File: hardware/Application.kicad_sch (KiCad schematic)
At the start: 32 parts, among them J501 Conn_ARM_SWD_TagConnect_TC203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, J502 Conn_ARM_SWD_TagConnect_TC2030, J503 BOOT0, U501 STM32G431CBU6, U502 W25X10CLUXIG, Y501 32_Mhz

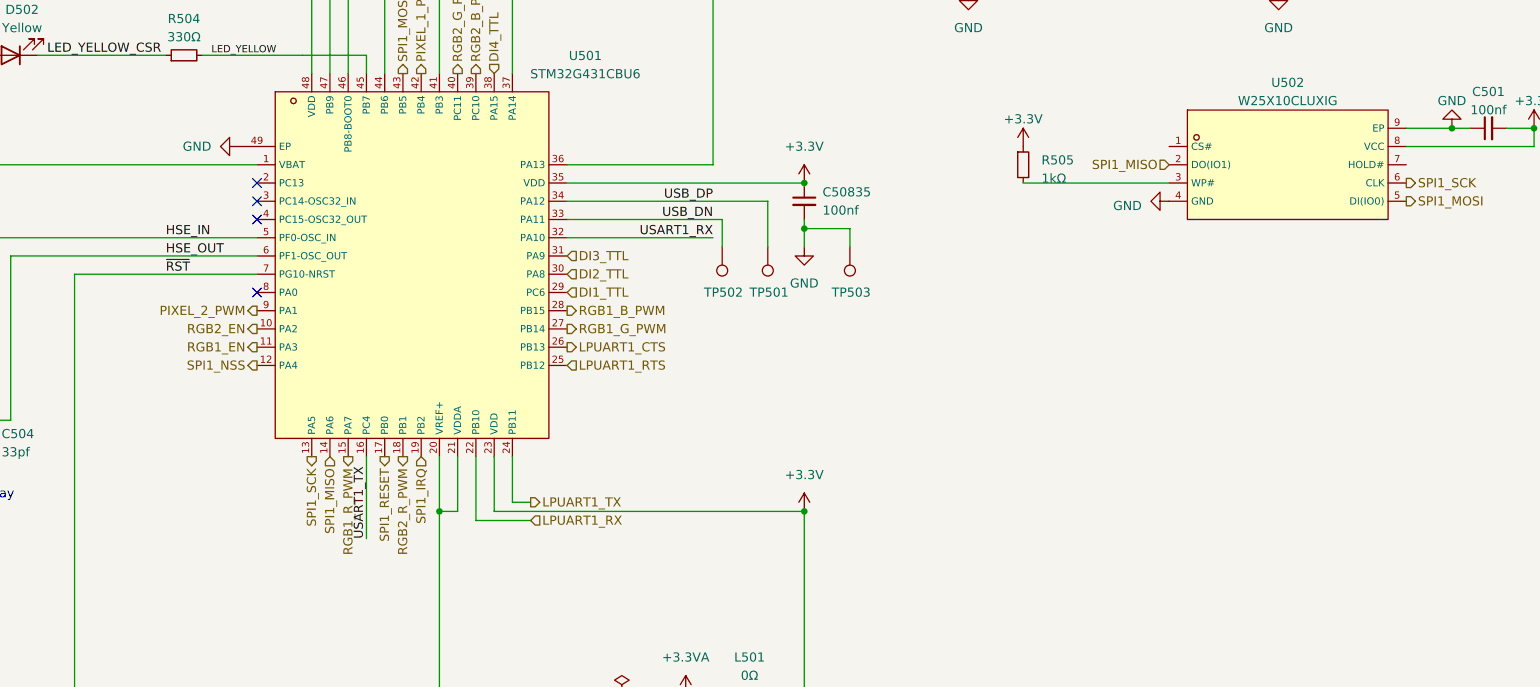
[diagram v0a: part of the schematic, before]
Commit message: hardware: add USB for debugging and programming
Signed-off-by: Connor Rigby <connorr@hey.com>
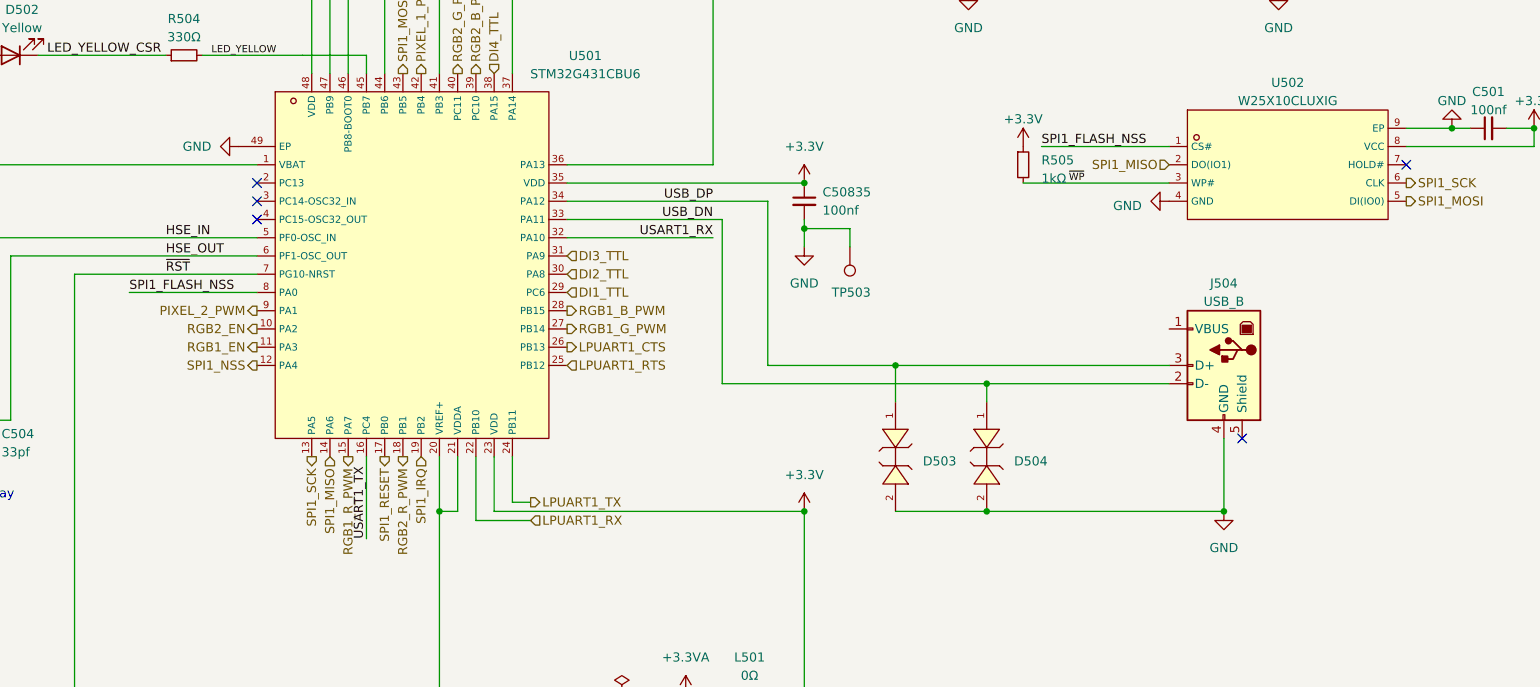
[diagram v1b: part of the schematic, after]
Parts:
- removed TP501: DP, TestPoint:TestPoint_Pad_D1.0mm, symbol Connector:TestPoint
- removed TP502: DN, TestPoint:TestPoint_Pad_D1.0mm, symbol Connector:TestPoint
- added D503, D504: ESD9B3_3ST5G, LCSC_ESD:SOD-923_L0.8-W0.6-LS1.0-BI-1, symbol LCSC_ESD:ESD9B3_3ST5G
- added J504: USB_B, LCSC_Connector:USB-B-TH_67068-8000, symbol Connector:USB_B
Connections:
- net GND: now also D503.2, D504.2, J504.4 (GND)
- net USB_DN: now also D504.1, J504.2 (D-)
- net USB_DP: now also D503.1, J504.3 (D+)
- net SPI1_FLASH_NSS: now reaches U502.1 (CS#)
- net SPI1_FLASH_NSS: now also U501.8 (PA0)
- net ~{WP}: now reaches R505.2, U502.3 (WP#)
- no-connect marks 8 -> 9

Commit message: Rev 2 submitted for production
Signed-off-by: Connor Rigby <connorr@hey.com>
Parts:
- removed BTN501, BTN502: GT-TC029B-H025-L1N, Button:SW-SMD_L3.9-W3.0-P4.45, symbol LCSC_Tactile_Switch:GT-TC029B-H025-L1N
- removed C501, C50823, C50835, C50848: C_0402_100nf_X7R, Capacitor_SMD:C_0402_1005Metric, symbol LCSC_Capacitor:C_0402_100nf_X7R
- removed C503, C504: C_0402_33p_C0G, Capacitor_SMD:C_0402_1005Metric, symbol LCSC_Capacitor:C_0402_33p_C0G
- removed C506: C_0402_1u_X5R, Capacitor_SMD:C_0402_1005Metric, symbol LCSC_Capacitor:C_0402_1u_X5R
- removed C509: C_0805_10u_X5R, Capacitor_SMD:C_0805_2012Metric, symbol LCSC_Capacitor:C_0805_10u_X5R
- removed D501: LED_0603_GREEN, LED_SMD:LED_0603_1608Metric, symbol LCSC_LED:LED_0603_GREEN
- removed D502: LED_0603_YELLOW, LED_SMD:LED_0603_1608Metric, symbol LCSC_LED:LED_0603_YELLOW
- removed D503, D504: ESD9B3_3ST5G, LCSC_ESD:SOD-923_L0.8-W0.6-LS1.0-BI-1, symbol LCSC_ESD:ESD9B3_3ST5G
- removed J501: Conn_ARM_SWD_TagConnect_TC2030-NL, Connector:Tag-Connect_TC2030-IDC-NL_2x03_P1.27mm_Vertical, symbol Connector:Conn_ARM_SWD_TagConnect_TC2030-NL
- removed J502: Conn_ARM_SWD_TagConnect_TC2030, Connector:Tag-Connect_TC2030-IDC-FP_2x03_P1.27mm_Vertical, symbol Connector:Conn_ARM_SWD_TagConnect_TC2030
- removed J503: BOOT0, Connector_PinHeader_2.54mm:PinHeader_1x02_P2.54mm_Vertical, symbol Connector_Generic:Conn_01x02
- removed J504: USB_B, LCSC_Connector:USB-B-TH_67068-8000, symbol Connector:USB_B
- removed L501: R_0402_0, Resistor_SMD:R_0402_1005Metric, symbol LCSC_Resistor:R_0402_0
- removed R501, R505: R_0402_1k, Resistor_SMD:R_0402_1005Metric, symbol LCSC_Resistor:R_0402_1k
- removed R502: R_0402_10k, Resistor_SMD:R_0402_1005Metric, symbol LCSC_Resistor:R_0402_10k
- removed R503, R504: R_0603_330, Resistor_SMD:R_0603_1608Metric, symbol LCSC_Resistor:R_0603_330
- removed TP503: GND, TestPoint:TestPoint_Pad_D1.0mm, symbol Connector:TestPoint
- removed U501: STM32G431CBU6, LCSC_Microcontroller:QFN50P700X700X60-49N, symbol LCSC_Microcontroller:STM32G431CBU6
- removed U502: W25X10CLUXIG, LCSC_Microcontroller:USON-8_L3.0-W2.0-P0.50-BL-EP-1, symbol LCSC_Microcontroller:W25X10CLUXIG
- removed Y501: 32_Mhz, Crystal:Crystal_SMD_3225-4Pin_3.2x2.5mm, symbol LCSC_Crystal:32_Mhz
- added BT501: Battery_Cell, LCSC_Connector:BAT-SMD_CR1220-2, symbol Device:Battery_Cell
- added C501: C_0805_4u7_X5R, Capacitor_SMD:C_0805_2012Metric, symbol LCSC_Capacitor:C_0805_4u7_X5R
- added C502, C503, C504, C506, C509, C516, C519, C520, C521: C_0402_100nf_X7R, Capacitor_SMD:C_0402_1005Metric, symbol LCSC_Capacitor:C_0402_100nf_X7R
- added C512, C513: C_0402_2u2_X5R, Capacitor_SMD:C_0402_1005Metric, symbol LCSC_Capacitor:C_0402_2u2_X5R
- added C811 (x4): C_0402_22p_C0G, Capacitor_SMD:C_0402_1005Metric, symbol LCSC_Capacitor:C_0402_22p_C0G
- added D202: 30v 230mv@100ma 1A, Diode_SMD:D_SOD-323F, symbol Device:D_Schottky
- added D501: BAT54C, Package_TO_SOT_SMD:SOT-23, symbol Diode:BAT54C
- added D502: LED_0603_GREEN, LED_SMD:LED_0603_1608Metric, symbol LCSC_LED:LED_0603_GREEN
- added D503: LED_0603_YELLOW, LED_SMD:LED_0603_1608Metric, symbol LCSC_LED:LED_0603_YELLOW
- added D504, D506: LED_0603_RED, LED_SMD:LED_0603_1608Metric, symbol LCSC_LED:LED_0603_RED
- added FB501: FerriteBead_Small, Inductor_SMD:L_0402_1005Metric, symbol Device:FerriteBead_Small
- added J501: Conn_ST_STDC14, LCSC_Connector:TC2070-IDC-FP, symbol Connector:Conn_ST_STDC14
- added JP501: SolderJumper_3_Open, Jumper:SolderJumper-3_P1.3mm_Open_RoundedPad1.0x1.5mm_NumberLabels, symbol Jumper:SolderJumper_3_Open
- added R501: R_0402_100k, Resistor_SMD:R_0402_1005Metric, symbol LCSC_Resistor:R_0402_100k
- added R502: R_0402_0, Resistor_SMD:R_0402_1005Metric, symbol LCSC_Resistor:R_0402_0
- added R503, R504, R505: R_0402_10k, Resistor_SMD:R_0402_1005Metric, symbol LCSC_Resistor:R_0402_10k
- added R506, R507, R508, R509: R_0603_330, Resistor_SMD:R_0603_1608Metric, symbol LCSC_Resistor:R_0603_330
- added RN501, RN502, RN503, RN504: RA_0402_04_100, Resistor_SMD:R_Array_Concave_4x0402, symbol LCSC_Resistor:RA_0402_04_100
- added U501: W25Q16JVSSIQ, Package_SO:SOIC-8_5.23x5.23mm_P1.27mm, symbol LCSC_Microcontroller:W25Q16JVSSIQ
- added U503: STM32F407VGTx, Package_QFP:LQFP-100_14x14mm_P0.5mm, symbol MCU_ST_STM32F4:STM32F407VGTx
- added Y501: 25_Mhz, Crystal:Crystal_SMD_3225-4Pin_3.2x2.5mm, symbol LCSC_Crystal:25_Mhz
- added Y502: Q13FC1350000400, Crystal:Crystal_SMD_3215-2Pin_3.2x1.5mm, symbol LCSC_Crystal:Q13FC1350000400
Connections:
- net +3.3V is gone; now on net GND: C508.2
- net BOOT0: now also R501.1, U503.94 (BOOT0)
- net CAN_RX: now also U503.91 (PB5)
- net CAN_TX: now also U503.52 (PB13)
- net GND: now also C507.2, C511.2, BT501.2 (-), C501.2, C502.2, C503.2, C504.2, C506.2, C509.2, C512.1, C513.1, C516.2, C519.2, C520.2, C521.2, C811.1, C811.1, C811.1, C811.1, J501.11 (GNDDetect), J501.5 (GND), J501.7 (GND), R501.2, U501.4 (GND), U503.10 (VSS), U503.20 (VSSA), U503.27 (VSS), U503.74 (VSS), U503.99 (VSS), Y501.2, Y501.4; no longer C507.1, C508.1, C511.1
- net USART1_RX: now also J501.13 (VCP_RX), U503.69 (PA10)
- net USART1_TX: now also J501.14 (VCP_TX), U503.68 (PA9)
- net ~{RST}: now also C516.1, JP501.3 (B), U503.14 (NRST); no longer C505.1
- removed net +3.3VA: C507.2, C510.1, C511.2
- new net: D504.2 (A), R509.1
- new net: C520.1, D202.1 (K), J501.3 (VCC)
- new net: D506.2 (A), R508.1
- new net +BATT: C509.1, D501.3, U503.6 (VBAT)
- new net CH1_B_PWM: RN502.7 (R2.2)
- new net CH1_EN_PWM: R508.2, RN502.8 (R1.2)
- new net CH1_G_PWM: RN502.6 (R3.2)
- new net CH1_NZR: RN503.1 (R1.1)
- new net CH1_R_PWM: RN502.5 (R4.2)
- new net CH2_B_PWM: RN501.7 (R2.2)
- new net CH2_EN_PWM: R509.2, RN501.8 (R1.2)
- new net CH2_G_PWM: RN501.6 (R3.2)
- new net CH2_NZR: RN503.2 (R2.1)
- new net CH2_R_PWM: RN501.5 (R4.2)
- new net FLASH_HOLD: R505.2, U501.7 (IO3)
- new net FLASH_SCK: R502.1, U501.6 (CLK)
- new net FLASH_WP: R504.2, U501.3 (IO2)
- new net GPIO_EXTI0: RN504.8 (R1.2), U503.15 (PC0)
- new net GPIO_EXTI1: RN504.7 (R2.2), U503.16 (PC1)
- new net GPIO_EXTI2: RN504.6 (R3.2), U503.17 (PC2)
- new net GPIO_EXTI3: RN504.5 (R4.2), U503.18 (PC3)
- new net HCI_CTS: U503.84 (PD3)
- new net HCI_EN: U503.83 (PD2)
- new net HCI_RTS: U503.85 (PD4)
- new net HCI_RX: U503.87 (PD6)
- new net HCI_TX: U503.86 (PD5)
- new net PI1: RN504.1 (R1.1)
- new net PI2: RN504.2 (R2.1)
- new net PI3: RN504.3 (R3.1)
- new net PI4: RN504.4 (R4.1)
- new net RADIO_IRQ: U503.7 (PC13)
- new net RADIO_MISO: U503.31 (PA6)
- new net RADIO_MOSI: U503.32 (PA7)
- new net RADIO_NSS: U503.29 (PA4)
- new net RADIO_SCK: U503.30 (PA5)
- new net RCC_OSC32_IN: C811.2, U503.8 (PC14), Y502.1
- new net RCC_OSC32_OUT: C811.2, U503.9 (PC15), Y502.2
- new net RCC_OSC_IN: C811.2, U503.12 (PH0), Y501.1
- new net RCC_OSC_OUT: C811.2, U503.13 (PH1), Y501.3
- new net SPI3_MISO: U501.2 (DO(IO1)), U503.79 (PC11)
- new net SPI3_MOSI: U501.5 (DI(IO0)), U503.80 (PC12)
- new net SPI3_NSS: R503.2, U501.1 (~{CS}), U503.34 (PC5)
- new net SPI3_SCK: R502.2, U503.78 (PC10)
- new net STATUS_RX: D503.1 (K), R507.2
- new net STATUS_RX_1: R507.1, RN503.4 (R4.1)
- new net STATUS_TX: D502.1 (K), R506.2
- new net STATUS_TX_1: R506.1, RN503.3 (R3.1)
- new net SYS_JTCK: J501.6 (JCLK/SWCLK), U503.76 (PA14)
- new net SYS_JTDI: J501.10 (JTDI/NC), U503.77 (PA15)
- new net SYS_JTDO: J501.8 (JTDO/SWO), U503.89 (PB3)
- new net SYS_JTMS: J501.4 (JTMS/SWDIO), U503.72 (PA13)
- new net SYS_TRST: JP501.1 (A), U503.90 (PB4)
- new net TIM1_CH1: RN502.4 (R4.1), U503.40 (PE9)
- new net TIM1_CH2: RN502.3 (R3.1), U503.42 (PE11)
- new net TIM1_CH3: RN502.2 (R2.1), U503.44 (PE13)
- new net TIM1_CH4: RN502.1 (R1.1), U503.45 (PE14)
- new net TIM2_CH1: RN501.4 (R4.1), U503.23 (PA0)
- new net TIM2_CH2: RN501.3 (R3.1), U503.24 (PA1)
- new net TIM2_CH3: RN501.2 (R2.1), U503.25 (PA2)
- new net TIM2_CH4: RN501.1 (R1.1), U503.26 (PA3)
- new net TIM3_CH1: RN503.8 (R1.2), U503.63 (PC6)
- new net TIM3_CH2: RN503.7 (R2.2), U503.64 (PC7)
- new net TIM3_CH3: RN503.6 (R3.2), U503.65 (PC8)
- new net TIM3_CH4: RN503.5 (R4.2), U503.66 (PC9)
- new net VBAT: BT501.1 (+), D501.1
- new net VCAP1: C512.2, U503.49 (VCAP_1)
- new net VCAP2: C513.2, U503.73 (VCAP_2)
- new net VDD: C501.1, C502.1, C503.1, C504.1, C505.1, C506.1, C507.1, C508.1, C510.1, C521.1, D202.2 (A), D501.2, D502.2 (A), D503.2 (A), D504.1 (K), D506.1 (K), FB501.2, R503.1, R504.1, R505.1, U501.8 (VCC), U503.100 (VDD), U503.11 (VDD), U503.19 (VDD), U503.28 (VDD), U503.50 (VDD), U503.75 (VDD)
- new net VDDA: C511.1, C519.1, FB501.1, U503.21 (VREF+), U503.22 (VDDA)
- new net ~{DEBUG_RST}: J501.12 (~{RST}), JP501.2 (C)
- new net ~{RADIO_RESET}: U503.36 (PB1)
- no-connect marks 9 -> 39
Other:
- note removed: "CL = ((CX1 x CX2) / (CX1 + CX2)) + Cstray CX1 = CX2 = 2(CL - Cstray) 33pf = CX2 = 2(22pf - 2pf)"

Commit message: ughhhhhhhhhhhhhhhhhhhhhhhhhhhhhhhhhhhhhhhhhhhhhhhhhhh
Signed-off-by: Connor Rigby <connorr@hey.com>
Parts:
- removed BT501: Battery_Cell, LCSC_Connector:BAT-SMD_CR1220-2, symbol Device:Battery_Cell
- removed C501: C_0805_4u7_X5R, Capacitor_SMD:C_0805_2012Metric, symbol LCSC_Capacitor:C_0805_4u7_X5R
- removed C507, C508, C509, C511, C516, C519, C520, C521: C_0402_100nf_X7R, Capacitor_SMD:C_0402_1005Metric, symbol LCSC_Capacitor:C_0402_100nf_X7R
- removed C510: C_0402_1u_X5R, Capacitor_SMD:C_0402_1005Metric, symbol LCSC_Capacitor:C_0402_1u_X5R
- removed C512, C513: C_0402_2u2_X5R, Capacitor_SMD:C_0402_1005Metric, symbol LCSC_Capacitor:C_0402_2u2_X5R
- removed C811 (x4): C_0402_22p_C0G, Capacitor_SMD:C_0402_1005Metric, symbol LCSC_Capacitor:C_0402_22p_C0G
- removed D202: 30v 230mv@100ma 1A, Diode_SMD:D_SOD-323F, symbol Device:D_Schottky
- removed D501: BAT54C, Package_TO_SOT_SMD:SOT-23, symbol Diode:BAT54C
- removed D502: LED_0603_GREEN, LED_SMD:LED_0603_1608Metric, symbol LCSC_LED:LED_0603_GREEN
- removed D503: LED_0603_YELLOW, LED_SMD:LED_0603_1608Metric, symbol LCSC_LED:LED_0603_YELLOW
- removed D504, D506: LED_0603_RED, LED_SMD:LED_0603_1608Metric, symbol LCSC_LED:LED_0603_RED
- removed J501: Conn_ST_STDC14, LCSC_Connector:TC2070-IDC-FP, symbol Connector:Conn_ST_STDC14
- removed JP501: SolderJumper_3_Open, Jumper:SolderJumper-3_P1.3mm_Open_RoundedPad1.0x1.5mm_NumberLabels, symbol Jumper:SolderJumper_3_Open
- removed R501: R_0402_100k, Resistor_SMD:R_0402_1005Metric, symbol LCSC_Resistor:R_0402_100k
- removed R502: R_0402_0, Resistor_SMD:R_0402_1005Metric, symbol LCSC_Resistor:R_0402_0
- removed R503, R504, R505: R_0402_10k, Resistor_SMD:R_0402_1005Metric, symbol LCSC_Resistor:R_0402_10k
- removed R506, R507, R508, R509: R_0603_330, Resistor_SMD:R_0603_1608Metric, symbol LCSC_Resistor:R_0603_330
- removed RN501, RN502, RN503, RN504: RA_0402_04_100, Resistor_SMD:R_Array_Concave_4x0402, symbol LCSC_Resistor:RA_0402_04_100
- removed U501: W25Q16JVSSIQ, Package_SO:SOIC-8_5.23x5.23mm_P1.27mm, symbol LCSC_Microcontroller:W25Q16JVSSIQ
- removed U503: STM32F407VGTx, Package_QFP:LQFP-100_14x14mm_P0.5mm, symbol MCU_ST_STM32F4:STM32F407VGTx
- removed Y501: 25_Mhz, Crystal:Crystal_SMD_3225-4Pin_3.2x2.5mm, symbol LCSC_Crystal:25_Mhz
- removed Y502: Q13FC1350000400, Crystal:Crystal_SMD_3215-2Pin_3.2x1.5mm, symbol LCSC_Crystal:Q13FC1350000400
- added C501: C_0402_100nf_X7R, Capacitor_SMD:C_0402_1005Metric, symbol LCSC_Capacitor:C_0402_100nf_X7R
- added U502: STM32G431CBUx, Package_DFN_QFN:QFN-48-1EP_7x7mm_P0.5mm_EP5.6x5.6mm, symbol MCU_ST_STM32G4:STM32G431CBUx
- FB501: LCSC C102745 -> (none); MPN RTT020000FTH -> (none)
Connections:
- net +BATT: now also C501.1, U502.1 (VBAT)
- net GND: now also C501.2, U502.49 (VSS)
- net PI1: now also U502.8 (PA0)
- net PI2: now also U502.9 (PA1)
- net PI3: now also U502.10 (PA2)
- net PI4: now also U502.11 (PA3)
- net RCC_OSC32_IN: now also U502.3 (PC14)
- net RCC_OSC32_OUT: now also U502.4 (PC15)
- net RCC_OSC_IN: now also U502.5 (PF0)
- net RCC_OSC_OUT: now also U502.6 (PF1)
- net VDD: now also U502.23 (VDD), U502.35 (VDD), U502.48 (VDD); no longer C505.1, C506.1, FB501.2
- net VDDA: now also C505.1, C506.1, FB501.2, U502.20 (VREF+); no longer FB501.1
- new net: FB501.1, U502.21 (VDDA)
- new net BLE_CTS: U502.26 (PB13)
- new net BLE_RTS: U502.25 (PB12)
- new net BLE_RX: U502.22 (PB10)
- new net BLE_TX: U502.24 (PB11)
- new net B_PWM: U502.18 (PB1)
- new net G_PWM: U502.14 (PA6)
- new net JT.CK: U502.37 (PA14)
- new net JT.DI: U502.38 (PA15)
- new net JT.DO: U502.41 (PB3)
- new net JT.MS: U502.36 (PA13)
- new net JT.RST: U502.42 (PB4)
- new net RGB_SENSE: U502.15 (PA7)
- new net RX_LED: U502.34 (PA12)
- new net R_PWM: U502.12 (PA4)
- new net TX_LED: U502.33 (PA11)
- new net VCP_RX: U502.32 (PA10)
- new net VCP_TX: U502.31 (PA9)
- new net ~{RESET}: U502.7 (PG10)
- no-connect marks 39 -> 16

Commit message: asdf
Signed-off-by: Connor Rigby <connorr@hey.com>
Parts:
- added C507, C508, C509, C510: C_0402_DNP, Capacitor_SMD:C_0402_1005Metric, symbol LCSC_Capacitor:C_0402_DNP
- added D501: LED_0603_YELLOW, LED_SMD:LED_0603_1608Metric, symbol LCSC_LED:LED_0603_YELLOW
- added D502: LED_0603_GREEN, LED_SMD:LED_0603_1608Metric, symbol LCSC_LED:LED_0603_GREEN
- added R501, R502: R_0603_DNP, Resistor_SMD:R_0603_1608Metric, symbol LCSC_Resistor:R_0603_DNP
- added Y501: 32_Mhz, Crystal:Crystal_SMD_3225-4Pin_3.2x2.5mm, symbol LCSC_Crystal:32_Mhz
- added Y502: Q13FC1350000400, footprint:FC-135R_L3.2-W1.5, symbol LCSC_Crystal:Q13FC1350000400
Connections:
- net GND: now also C507.2, C508.2, C509.2, C510.2, Y501.2, Y501.4
- net RCC_OSC32_IN: now also C509.1, Y502.1
- net RCC_OSC32_OUT: now also C510.1, Y502.2
- net RCC_OSC_IN: now also C507.1, Y501.1
- net RCC_OSC_OUT: now also C508.1, Y501.3
- net RX_LED: now also D502.1 (K)
- net TX_LED: now also D501.1 (K)
- net VDD: now also R501.2, R502.2
- net BLE_CTS renamed HCI.CTS
- net BLE_RTS renamed HCI.RTS
- net BLE_RX renamed HCI.RX
- net BLE_TX renamed HCI.TX
- net RGB_SENSE: no longer names the net of U502.15 (PA7)
- new net: D501.2 (A), R501.1
- new net: D502.2 (A), R502.1
- no-connect marks 16 -> 17
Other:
- moved on the sheet: C501, C502, C503, C504, C505, C506, FB501, U502

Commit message: updates
Signed-off-by: Connor Rigby <connorr@hey.com>
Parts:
- added C511: C_0805_4u7_X5R, Capacitor_SMD:C_0805_2012Metric, symbol LCSC_Capacitor:C_0805_4u7_X5R
- FB501: footprint Inductor_SMD:L_0402_1005Metric -> Inductor_SMD:L_0603_1608Metric
- Y502: footprint footprint:FC-135R_L3.2-W1.5 -> Crystal:Crystal_SMD_3215-2Pin_3.2x1.5mm
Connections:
- net GND: now also C511.2
- net NZR1_PWM: now also U502.44 (PB6)
- net NZR2_PWM: now also U502.45 (PB7)
- net VDD: now also C505.1, FB501.2, C511.1
- net VDDA: now also FB501.1, U502.21 (VDDA); no longer C505.1, FB501.2
- net CAN_RX: now reaches U502.46 (PB8)
- net CAN_TX: now reaches U502.47 (PB9)
- no-connect marks 17 -> 13
